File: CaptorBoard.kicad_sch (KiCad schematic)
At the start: 24 parts, among them J1 Conn_01x06, J2 MKDSN 1,5/ 4-5,08, SW1 SKHHLVA010, SW2 SKHHLVA010, U1 WeMos_mini, U2 IRM-02-5, U3 MOC3040X, U4 MOC3040X, U5 DHT22

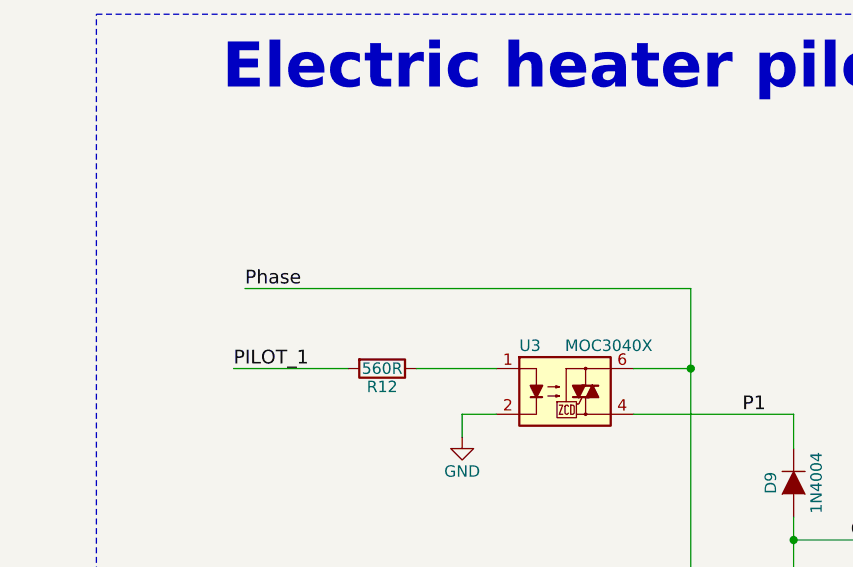
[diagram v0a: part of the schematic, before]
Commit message: add pull up for booting conditions
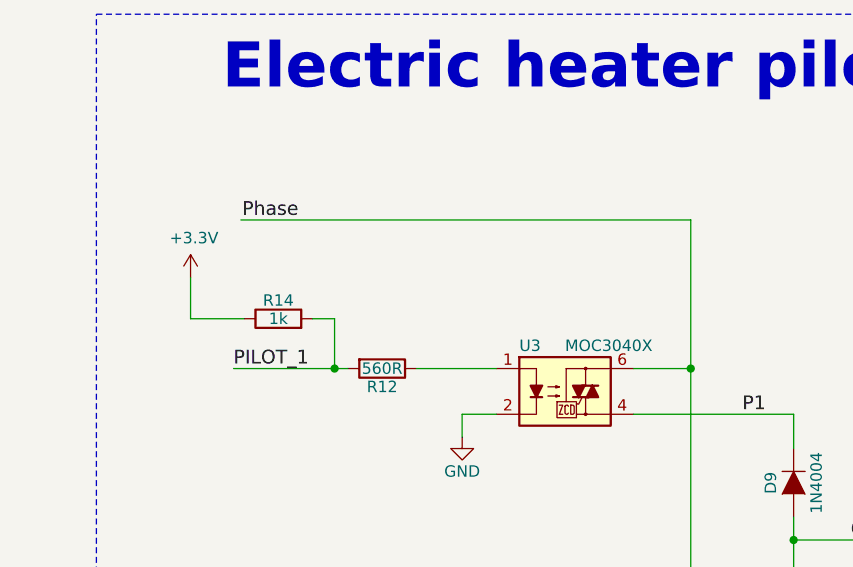
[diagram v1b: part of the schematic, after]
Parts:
- added R14: 1k, Resistor_SMD:R_1210_3225Metric_Pad1.42x2.65mm_HandSolder, symbol CaptorBoard-rescue:R-device
- D10, D9: footprint Diodes_THT:D_DO-41_SOD81_P7.62mm_Horizontal -> Diode_THT:D_DO-41_SOD81_P7.62mm_Horizontal
- D3, D4, D5, D6, D7: footprint LEDs:LED_D3.0mm -> LED_THT:LED_D3.0mm
- J1: footprint Pin_Headers:Pin_Header_Straight_1x06_Pitch2.54mm -> Connector_PinHeader_2.54mm:PinHeader_1x06_P2.54mm_Vertical
- J2: footprint TerminalBlocks_Phoenix:TerminalBlock_Phoenix_MKDS1.5-4pol -> TerminalBlock_Phoenix:TerminalBlock_Phoenix_MKDS-1,5-4-5.08_1x04_P5.08mm_Horizontal
- R10, R11, R12, R13, R7, R8, R9: footprint Resistors_SMD:R_1210_HandSoldering -> Resistor_SMD:R_1210_3225Metric_Pad1.42x2.65mm_HandSolder
- SW1, SW2: footprint Buttons_Switches_THT:SW_Tactile_SKHH_Angled -> Button_Switch_THT:SW_Tactile_SKHH_Angled
- U2: footprint Converters_DCDC_ACDC:ACDC-Conv_THTMeanWell-IRM-02-XX -> Converter_ACDC:Converter_ACDC_MeanWell_IRM-02-xx_THT
- U3, U4: footprint Housings_DIP:DIP-6_W7.62mm -> Package_DIP:DIP-6_W7.62mm
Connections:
- net +3V3: now also R14.1
- net PILOT_1: now also R14.2

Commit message: with new kicad version
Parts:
- added R15: 1k, Resistor_SMD:R_1210_3225Metric_Pad1.42x2.65mm_HandSolder, symbol CaptorBoard-rescue:R-device
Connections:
- net +3V3: now also R15.1
- net PILOT_2: now also R15.2
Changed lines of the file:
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@@
   (junction (at 97.79 161.29) (diameter 0.9144) (color 0 0 0 0))
   (junction (at 104.14 236.22) (diameter 0.9144) (color 0 0 0 0))
+  (junction (at 310.7436 231.14) (diameter 0.9144) (color 0 0 0 0))
   (junction (at 310.9468 201.93) (diameter 0.9144) (color 0 0 0 0))
   (junction (at 350.52 201.93) (diameter 0.9144) (color 0 0 0 0))
@@
     (stroke (width 0) (type solid) (color 0 0 0 0))
   )
+  (wire (pts (xy 295.1988 216.8652) (xy 295.1988 223.2152))
+    (stroke (width 0) (type solid) (color 0 0 0 0))
+  )
+  (wire (pts (xy 295.1988 223.2152) (xy 300.4312 223.2152))
+    (stroke (width 0) (type solid) (color 0 0 0 0))
+  )
   (wire (pts (xy 300.5328 185.42) (xy 350.52 185.42))
     (stroke (width 0) (type solid) (color 0 0 0 0))
@@
     (stroke (width 0) (type solid) (color 0 0 0 0))
   )
+  (wire (pts (xy 310.7436 223.2152) (xy 308.0512 223.2152))
+    (stroke (width 0) (type solid) (color 0 0 0 0))
+  )
+  (wire (pts (xy 310.7436 231.14) (xy 298.45 231.14))
+    (stroke (width 0) (type solid) (color 0 0 0 0))
+  )
+  (wire (pts (xy 310.7436 231.14) (xy 310.7436 223.2152))
+    (stroke (width 0) (type solid) (color 0 0 0 0))
+  )
   (wire (pts (xy 310.9468 196.3928) (xy 308.5084 196.3928))
     (stroke (width 0) (type solid) (color 0 0 0 0))
@@
     (stroke (width 0) (type solid) (color 0 0 0 0))
   )
-  (wire (pts (xy 312.42 231.14) (xy 298.45 231.14))
+  (wire (pts (xy 312.42 231.14) (xy 310.7436 231.14))
     (stroke (width 0) (type solid) (color 0 0 0 0))
   )
@@
     )
     (property "Datasheet" "" (id 3) (at 294.9448 191.8208 0)
+      (effects (font (size 1.27 1.27)) hide)
+    )
+  )
+  (symbol (lib_id "CaptorBoard-rescue:+3.3V-power") (at 295.1988 216.8652 0) (unit 1)
+    (in_bom yes) (on_board yes)
+    (property "Reference" "#PWR0104" (id 0) (at 295.1988 220.6752 0)
+      (effects (font (size 1.27 1.27)) hide)
+    )
+    (property "Value" "+3.3V" (id 1) (at 295.5798 212.471 0))
+    (property "Footprint" "" (id 2) (at 295.1988 216.8652 0)
+      (effects (font (size 1.27 1.27)) hide)
+    )
+    (property "Datasheet" "" (id 3) (at 295.1988 216.8652 0)
       (effects (font (size 1.27 1.27)) hide)
     )
@@
     )
   )
+  (symbol (lib_id "CaptorBoard-rescue:R-device") (at 304.2412 223.2152 90) (unit 1)
+    (in_bom yes) (on_board yes)
+    (property "Reference" "R15" (id 0) (at 304.2414 221.1834 90))
+    (property "Value" "1k" (id 1) (at 304.2412 223.2152 90))
+    (property "Footprint" "Resistor_SMD:R_1210_3225Metric_Pad1.42x2.65mm_HandSolder" (id 2) (at 304.2412 224.9932 90)
+      (effects (font (size 0.762 0.762)) hide)
+    )
+    (property "Datasheet" "" (id 3) (at 304.2412 223.2152 0)
+      (effects (font (size 0.762 0.762)))
+    )
+  )
   (symbol (lib_id "CaptorBoard-rescue:R-device") (at 304.6984 196.3928 90) (unit 1)
     (in_bom yes) (on_board yes)
@@
       (reference "#PWR0103") (unit 1) (value "+3.3V") (footprint "")
     )
+    (path "/1cc8bda3-0f3b-4ad6-b594-ede9363d27c9"
+      (reference "#PWR0104") (unit 1) (value "+3.3V") (footprint "")
+    )
     (path "/00000000-0000-0000-0000-0000552596b4"
       (reference "D3") (unit 1) (value "POWER") (footprint "LED_THT:LED_D3.0mm")
@@
       (reference "R14") (unit 1) (value "1k") (footprint "Resistor_SMD:R_1210_3225Metric_Pad1.42x2.65mm_HandSolder")
     )
+    (path "/24cde26c-2d59-40a3-80d6-88dd1d5dc7c1"
+      (reference "R15") (unit 1) (value "1k") (footprint "Resistor_SMD:R_1210_3225Metric_Pad1.42x2.65mm_HandSolder")
+    )
     (path "/00000000-0000-0000-0000-00005525b6ce"
